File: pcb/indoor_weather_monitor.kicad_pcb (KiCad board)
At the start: 2 copper layers, 3 parts, among them U1 DOIT-ESP32-DEVKIT-V1, U2 4.0inch_SPI_MSP4021, U2_BME280 module_bme280

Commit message: tooling around with placement
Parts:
- added Ue: module_bh1750, usini_sensors:module_bh1750, F.Cu at (193.4, 86.1)
- U2_BME280: moved to F.Cu
- moved U2_BME280 43.5 mm to (189.8, 106.0), turned to 0 degrees
- moved U1 10.3 mm to (93.2, 94.6)
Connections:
- U1 pad 26: unconnected-(U1-Pad26) -> Net-(U1-Pad26)
- U1 pad 9: unconnected-(U1-Pad9) -> Net-(U1-Pad9)
- U2 pad 5: Net-(U1-Pad35) -> Net-(U1-Pad9)
- U2 pad 8: Net-(U1-Pad19) -> Net-(U1-Pad26)

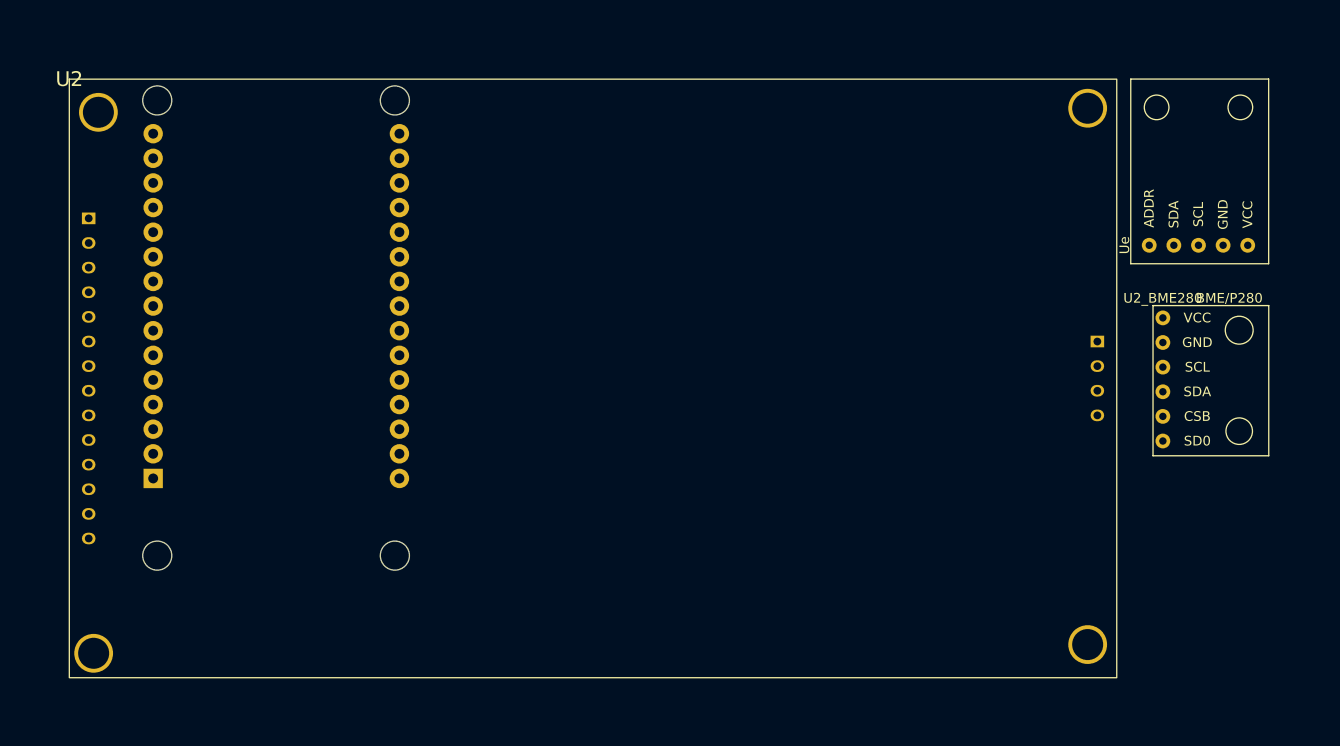
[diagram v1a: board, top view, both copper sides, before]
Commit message: repositioning local forecast
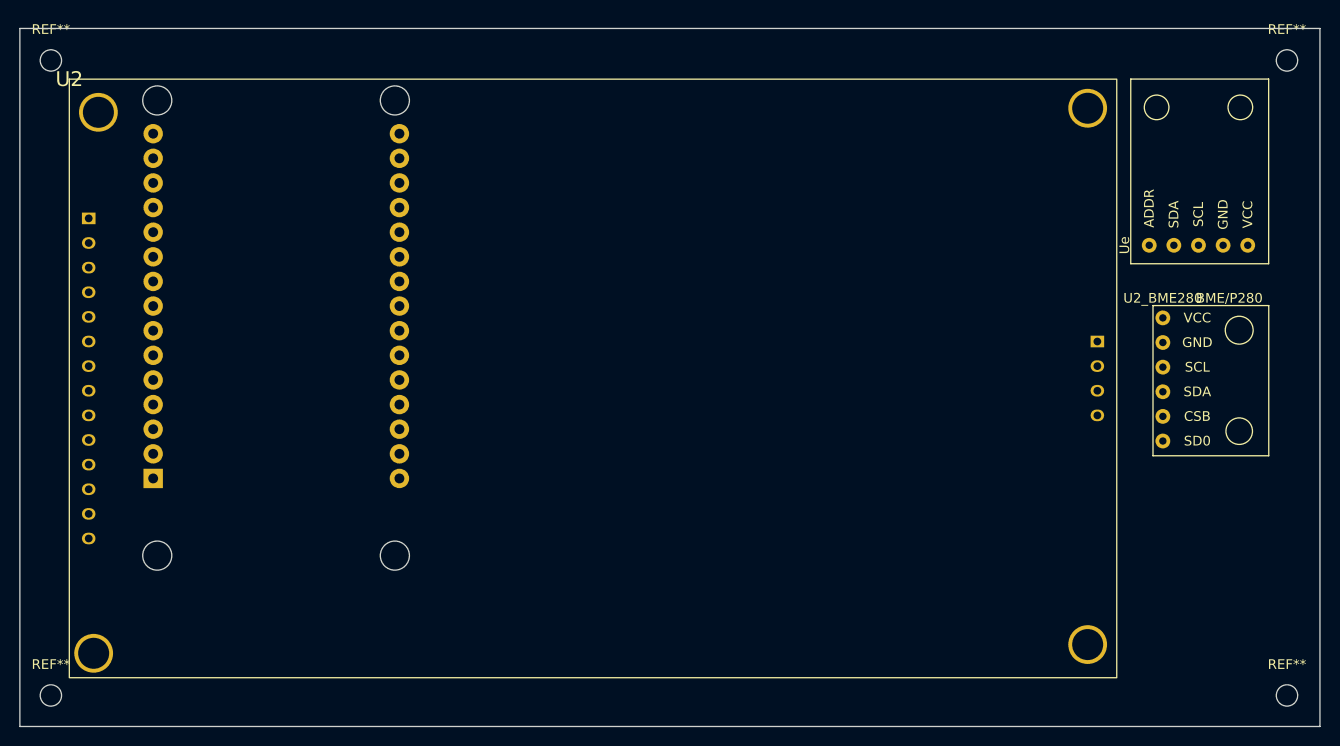
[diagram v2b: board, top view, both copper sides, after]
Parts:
- added REF**: MountingHole_2.2mm_M2, MountingHole:MountingHole_2.2mm_M2, F.Cu at (70.0, 132.5)
- added REF**: MountingHole_2.2mm_M2, MountingHole:MountingHole_2.2mm_M2, F.Cu at (197.5, 132.5)
- added REF**: MountingHole_2.2mm_M2, MountingHole:MountingHole_2.2mm_M2, F.Cu at (197.5, 67.0)
- added REF**: MountingHole_2.2mm_M2, MountingHole:MountingHole_2.2mm_M2, F.Cu at (70.0, 67.0)
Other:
- board outline added: 134.1 x 72 mm
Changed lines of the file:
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@@
     )
+  )
+  (footprint "MountingHole:MountingHole_2.2mm_M2" (layer "F.Cu")
+    (at 70 132.5)
+    (descr "Mounting Hole 2.2mm, no annular, M2")
+    (tags "mounting hole 2.2mm no annular m2")
+    (attr exclude_from_pos_files exclude_from_bom)
+    (fp_text reference "REF**" (at 0 -3.2) (layer "F.SilkS")
+      (effects (font (size 1 1) (thickness 0.15)))
+    )
+    (fp_text value "MountingHole_2.2mm_M2" (at 0 3.2) (layer "F.Fab")
+      (effects (font (size 1 1) (thickness 0.15)))
+    )
+    (fp_text user "${REFERENCE}" (at 0.3 0) (layer "F.Fab")
+      (effects (font (size 1 1) (thickness 0.15)))
+    )
+    (fp_circle (center 0 0) (end 2.2 0) (layer "Cmts.User") (width 0.15) (fill none))
+    (fp_circle (center 0 0) (end 2.45 0) (layer "F.CrtYd") (width 0.05) (fill none))
+    (pad "" np_thru_hole circle locked (at 0 0) (size 2.2 2.2) (drill 2.2) (layers *.Cu *.Mask))
+  )
+  (footprint "MountingHole:MountingHole_2.2mm_M2" (layer "F.Cu")
+    (at 197.5 132.5)
+    (descr "Mounting Hole 2.2mm, no annular, M2")
+    (tags "mounting hole 2.2mm no annular m2")
+    (attr exclude_from_pos_files exclude_from_bom)
+    (fp_text reference "REF**" (at 0 -3.2) (layer "F.SilkS")
+      (effects (font (size 1 1) (thickness 0.15)))
+    )
+    (fp_text value "MountingHole_2.2mm_M2" (at 0 3.2) (layer "F.Fab")
+      (effects (font (size 1 1) (thickness 0.15)))
+    )
+    (fp_text user "${REFERENCE}" (at 0.3 0) (layer "F.Fab")
+      (effects (font (size 1 1) (thickness 0.15)))
+    )
+    (fp_circle (center 0 0) (end 2.2 0) (layer "Cmts.User") (width 0.15) (fill none))
+    (fp_circle (center 0 0) (end 2.45 0) (layer "F.CrtYd") (width 0.05) (fill none))
+    (pad "" np_thru_hole circle locked (at 0 0) (size 2.2 2.2) (drill 2.2) (layers *.Cu *.Mask))
+  )
+  (footprint "MountingHole:MountingHole_2.2mm_M2" (layer "F.Cu")
+    (at 197.5 67)
+    (descr "Mounting Hole 2.2mm, no annular, M2")
+    (tags "mounting hole 2.2mm no annular m2")
+    (attr exclude_from_pos_files exclude_from_bom)
+    (fp_text reference "REF**" (at 0 -3.2) (layer "F.SilkS")
+      (effects (font (size 1 1) (thickness 0.15)))
+    )
+    (fp_text value "MountingHole_2.2mm_M2" (at 0 3.2) (layer "F.Fab")
+      (effects (font (size 1 1) (thickness 0.15)))
+    )
+    (fp_text user "${REFERENCE}" (at 0.3 0) (layer "F.Fab")
+      (effects (font (size 1 1) (thickness 0.15)))
+    )
+    (fp_circle (center 0 0) (end 2.2 0) (layer "Cmts.User") (width 0.15) (fill none))
+    (fp_circle (center 0 0) (end 2.45 0) (layer "F.CrtYd") (width 0.05) (fill none))
+    (pad "" np_thru_hole circle locked (at 0 0) (size 2.2 2.2) (drill 2.2) (layers *.Cu *.Mask))
   )
   (footprint "lcd:4.0inch_SPI" (layer "F.Cu")
@@
     (pad "14" thru_hole oval (at 2 47.38 270) (size 1.2 1.4) (drill 0.8) (layers *.Cu *.Mask)
       (net 38 "unconnected-(U2-Pad14)") (pinfunction "T_IRQ") (pintype "input"))
+  )
+  (footprint "MountingHole:MountingHole_2.2mm_M2" (layer "F.Cu")
+    (at 70 67)
+    (descr "Mounting Hole 2.2mm, no annular, M2")
+    (tags "mounting hole 2.2mm no annular m2")
+    (attr exclude_from_pos_files exclude_from_bom)
+    (fp_text reference "REF**" (at 0 -3.2) (layer "F.SilkS")
+      (effects (font (size 1 1) (thickness 0.15)))
+    )
+    (fp_text value "MountingHole_2.2mm_M2" (at 0 3.2) (layer "F.Fab")
+      (effects (font (size 1 1) (thickness 0.15)))
+    )
+    (fp_text user "${REFERENCE}" (at 0.3 0) (layer "F.Fab")
+      (effects (font (size 1 1) (thickness 0.15)))
+    )
+    (fp_circle (center 0 0) (end 2.2 0) (layer "Cmts.User") (width 0.15) (fill none))
+    (fp_circle (center 0 0) (end 2.45 0) (layer "F.CrtYd") (width 0.05) (fill none))
+    (pad "" np_thru_hole circle locked (at 0 0) (size 2.2 2.2) (drill 2.2) (layers *.Cu *.Mask))
   )
   (footprint "esp32:MODULE_ESP32_DEVKIT_V1" (layer "B.Cu")
@@
       (net 30 "Net-(U1-Pad30)") (pinfunction "GPIO18_VSPI-CLK") (pintype "bidirectional"))
   )
+  (gr_rect (start 66.8 63.7) (end 200.9 135.7) (layer "Edge.Cuts") (width 0.1) (fill none))
 )
